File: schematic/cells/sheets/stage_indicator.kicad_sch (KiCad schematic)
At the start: 11 parts, among them J1511 PORT_LOAD, Q1505 MMBT3904,215, Q1508 2N7002,215, U1503 OPA4196IDR

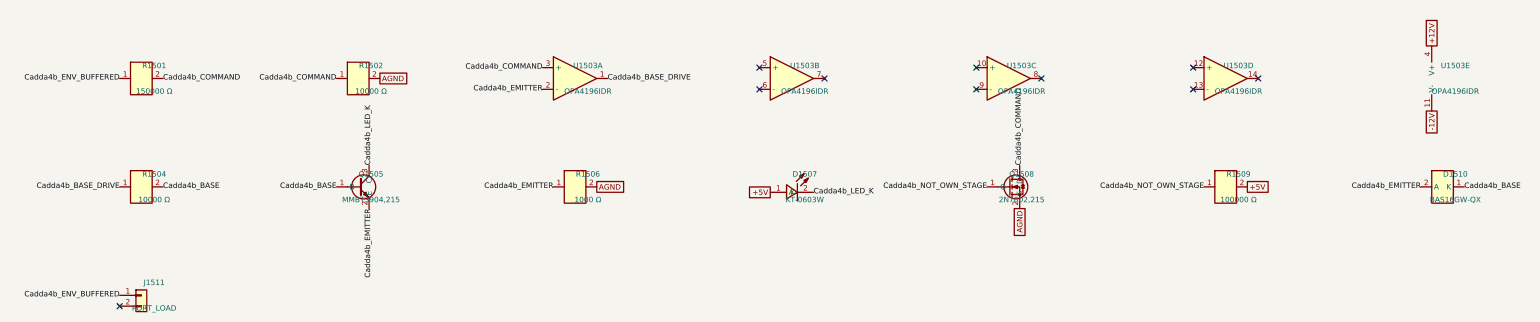
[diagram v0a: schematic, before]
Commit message: Close master schematic integration gates
Audit locked panel coverage, netlist parity, sensitive islands and all active units; terminate spare cells, refresh evidence, and record rail budget overshoot and draft exports.
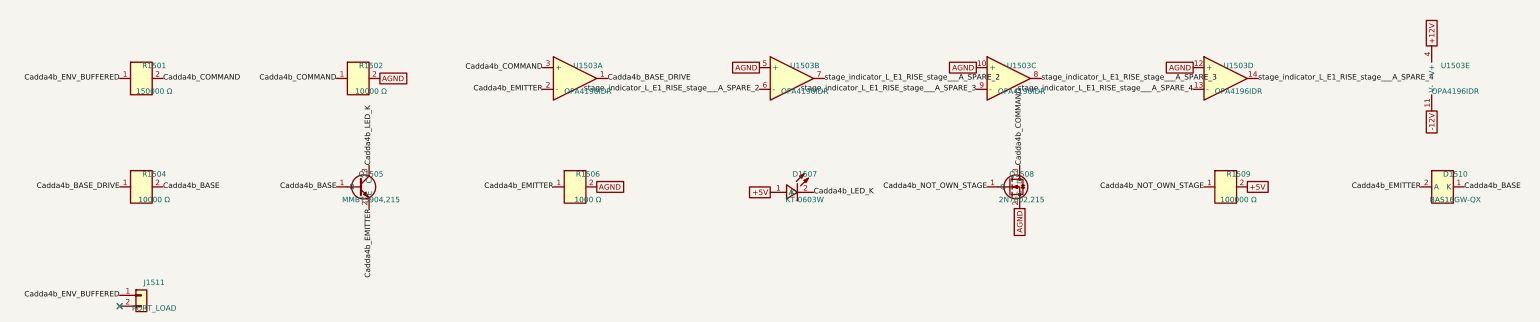
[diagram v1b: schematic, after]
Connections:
- net AGND: now also U1503.10 (+), U1503.12 (+), U1503.5 (+)
- net stage_indicator_L_E1_RISE_stage___A_SPARE_3: now reaches U1503.8
- net stage_indicator_L_E1_RISE_stage___A_SPARE_3: now also U1503.9 (-)
- net stage_indicator_L_E1_RISE_stage___A_SPARE_4: now reaches U1503.13 (-)
- net stage_indicator_L_E1_RISE_stage___A_SPARE_4: now also U1503.14
- net stage_indicator_L_E1_RISE_stage___A_SPARE_2: now reaches U1503.6 (-)
- net stage_indicator_L_E1_RISE_stage___A_SPARE_2: now also U1503.7
- no-connect marks 10 -> 1
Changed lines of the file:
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@@
     ))
   )
-  (no_connect (at 195.58 48.26))
-  (no_connect (at 195.58 53.34))
-  (no_connect (at 210.82 50.8))
+  (global_label "AGND" (shape passive) (at 195.58 48.26 0) (effects (font (size 1.27 1.27)) (justify right)))
+  (label "stage_indicator_L_E1_RISE_stage___A_SPARE_2" (at 195.58 53.34 0) (effects (font (size 1.27 1.27)) (justify right)))
+  (label "stage_indicator_L_E1_RISE_stage___A_SPARE_2" (at 210.82 50.8 180) (effects (font (size 1.27 1.27)) (justify left)))
   (symbol (lib_id "zudo-osc-hole-field:OPA4196IDR") (at 254 50.8 0) (unit 3)
     (exclude_from_sim no) (in_bom yes) (on_board yes) (dnp no)
@@
     ))
   )
-  (no_connect (at 261.62 50.8))
-  (no_connect (at 246.38 53.34))
-  (no_connect (at 246.38 48.26))
+  (label "stage_indicator_L_E1_RISE_stage___A_SPARE_3" (at 261.62 50.8 180) (effects (font (size 1.27 1.27)) (justify left)))
+  (label "stage_indicator_L_E1_RISE_stage___A_SPARE_3" (at 246.38 53.34 0) (effects (font (size 1.27 1.27)) (justify right)))
+  (global_label "AGND" (shape passive) (at 246.38 48.26 0) (effects (font (size 1.27 1.27)) (justify right)))
   (symbol (lib_id "zudo-osc-hole-field:OPA4196IDR") (at 304.8 50.8 0) (unit 4)
     (exclude_from_sim no) (in_bom yes) (on_board yes) (dnp no)
@@
     ))
   )
-  (no_connect (at 297.18 48.26))
-  (no_connect (at 297.18 53.34))
-  (no_connect (at 312.42 50.8))
+  (global_label "AGND" (shape passive) (at 297.18 48.26 0) (effects (font (size 1.27 1.27)) (justify right)))
+  (label "stage_indicator_L_E1_RISE_stage___A_SPARE_4" (at 297.18 53.34 0) (effects (font (size 1.27 1.27)) (justify right)))
+  (label "stage_indicator_L_E1_RISE_stage___A_SPARE_4" (at 312.42 50.8 180) (effects (font (size 1.27 1.27)) (justify left)))
   (symbol (lib_id "zudo-osc-hole-field:OPA4196IDR") (at 355.6 50.8 0) (unit 5)
     (exclude_from_sim no) (in_bom yes) (on_board yes) (dnp no)

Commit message: Select exact compact indicator LEDs and audit fixed centres
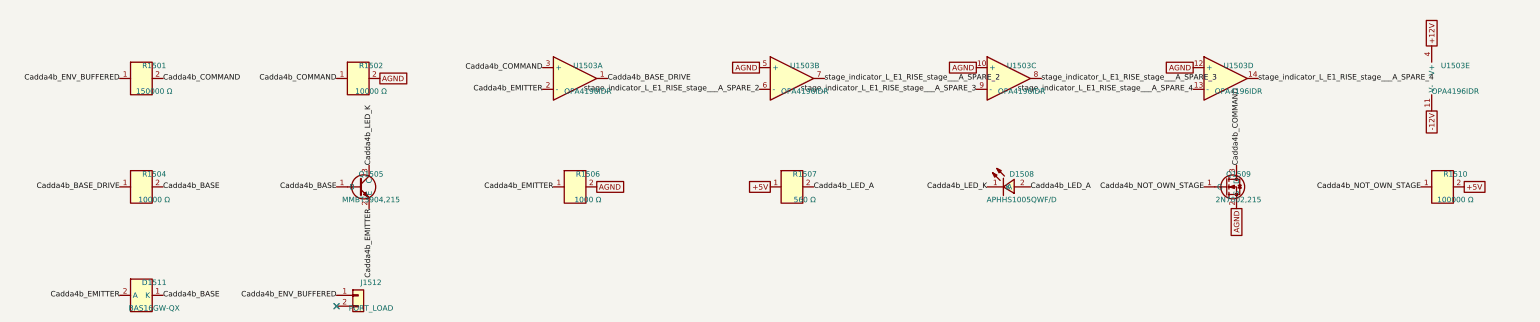
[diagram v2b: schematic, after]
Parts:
- removed J1511: PORT_LOAD, symbol Fixture:Conn_01x02
- added J1512: PORT_LOAD, symbol Fixture:Conn_01x02
- added R1507: 560 Ω, zudo-osc-hole-field:R0603, symbol zudo-osc-hole-field:RC0603FR-07100KL
- D1508: renamed from D1507; value KT-0603W -> APHHS1005QWF/D; footprint zudo-osc-hole-field:LED0603-R-RD_WHITE -> zudo-osc-hole-field:LED0402-Kingbright-White; symbol zudo-osc-hole-field:0603Whitelight_C2290 -> zudo-osc-hole-field:Kingbright_White_0402; LCSC C2290 -> (none); MPN KT-0603W -> APHHS1005QWF/D; Manufacturer KENTO -> Kingbright
- renumbered D1510 to D1511, Q1508 to Q1509, R1509 to R1510
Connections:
- net +5V: now also R1507.1; no longer D1508.1 (A)
- net Cadda4b_ENV_BUFFERED: now also J1512.1 (Pin_1)
- net Cadda4b_LED_K: now also D1508.1 (K); no longer D1508.2 (K)
- new net Cadda4b_LED_A: D1508.2 (A), R1507.2
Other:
- moved on the sheet: D1508, D1511, Q1509, R1510
